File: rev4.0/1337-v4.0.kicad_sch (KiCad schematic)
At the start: 53 parts, among them J1 USB_IN, J2 AVR-ISP-6, SW1 SW_Push, U1 SSD1306, U2 USBLC6-2SC6, U3 ATMEGA32U4, Y1 16MHz

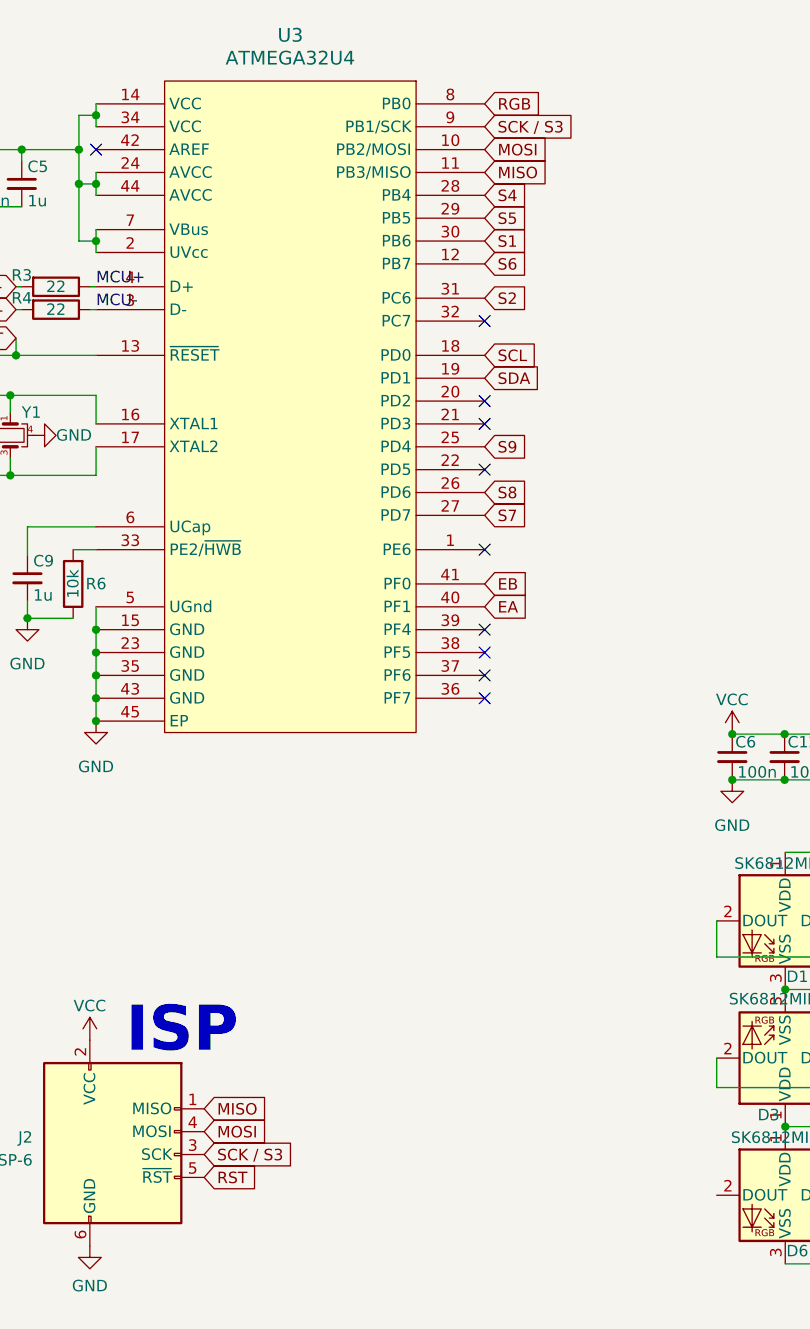
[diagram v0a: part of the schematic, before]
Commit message: added teardrops
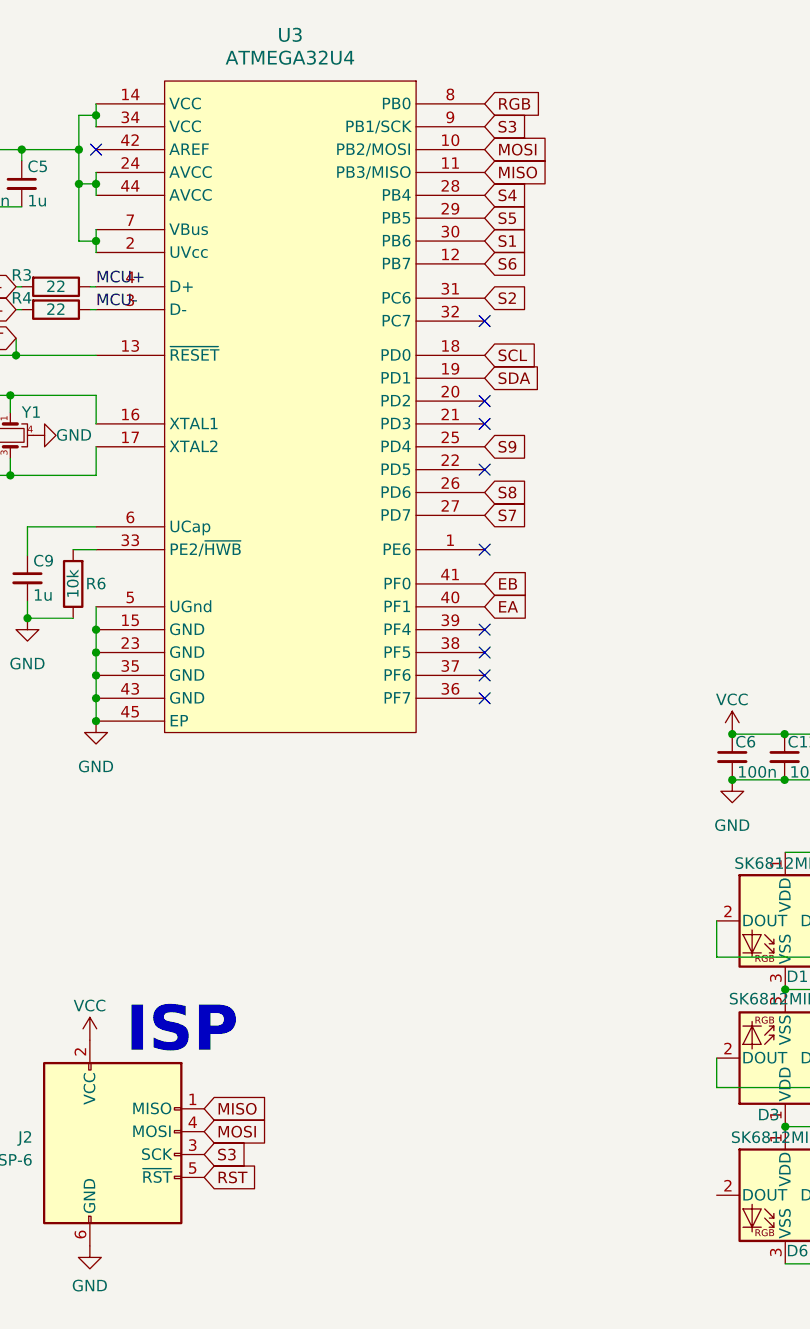
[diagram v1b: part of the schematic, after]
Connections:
- net SCK / S3 is gone; now on net S3: J2.3 (SCK), U3.9 (PB1/SCK)
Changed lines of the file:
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@@
     )
   )
-  (global_label "SCK {slash} S3" (shape input) (at 176.53 29.8196 0) (fields_autoplaced)
+  (global_label "S3" (shape input) (at 176.53 29.8196 0) (fields_autoplaced)
     (effects (font (size 1.27 1.27)) (justify left))
-    (property "Intersheet References" "${INTERSHEET_REFS}" (id 0) (at 188.5679 29.7402 0)
+    (property "Intersheet References" "${INTERSHEET_REFS}" (id 0) (at 181.5526 29.7402 0)
       (effects (font (size 1.27 1.27)) (justify left) hide)
     )
@@
     )
   )
-  (global_label "SCK {slash} S3" (shape input) (at 145.3642 144.018 0) (fields_autoplaced)
+  (global_label "S3" (shape input) (at 145.3642 144.018 0) (fields_autoplaced)
     (effects (font (size 1.27 1.27)) (justify left))
-    (property "Intersheet References" "${INTERSHEET_REFS}" (id 0) (at 157.4021 143.9386 0)
+    (property "Intersheet References" "${INTERSHEET_REFS}" (id 0) (at 150.3868 143.9386 0)
       (effects (font (size 1.27 1.27)) (justify left) hide)
     )
